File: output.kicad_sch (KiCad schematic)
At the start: 72 parts, among them Q10 AO4407A, Q11 2N7002, Q12 MMBT3904, Q13 2N7002, Q14 2N7002, Q15 2N7002, Q16 2N7002, Q17 2N7002, Q18 MMBT3904, Q19 AO4407A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

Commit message: Fix incorrect part number on R32
Previously chosen part had 0402 footprint, 0603 needed.
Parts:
- R32: LCSC C25792 -> C25819
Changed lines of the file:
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@@
       (effects (font (size 1.27 1.27)) hide)
     )
-    (property "LCSC" "C25792" (id 4) (at 102.87 119.38 0)
+    (property "LCSC" "C25819" (id 4) (at 102.87 119.38 0)
       (effects (font (size 1.27 1.27)) hide)
     )

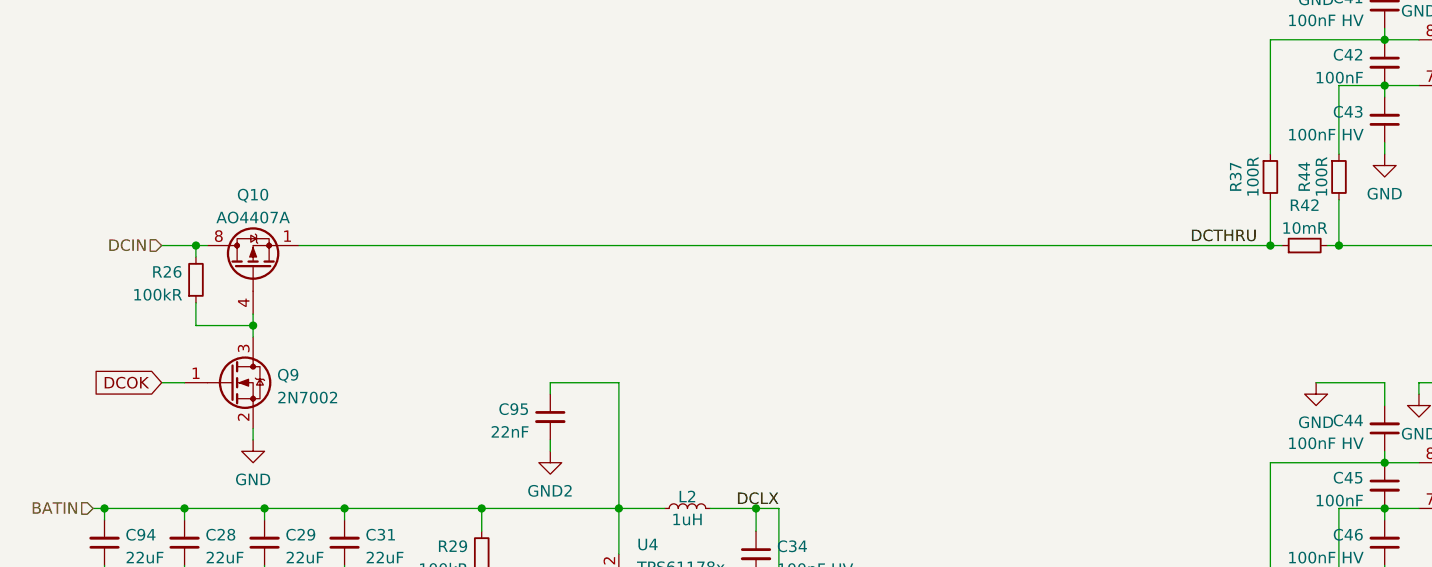
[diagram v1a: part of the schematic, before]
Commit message: Fix gate discharge resistor on Q10
The gate discharge resistor on Q10 was by mistake connected to drain
instead of source.
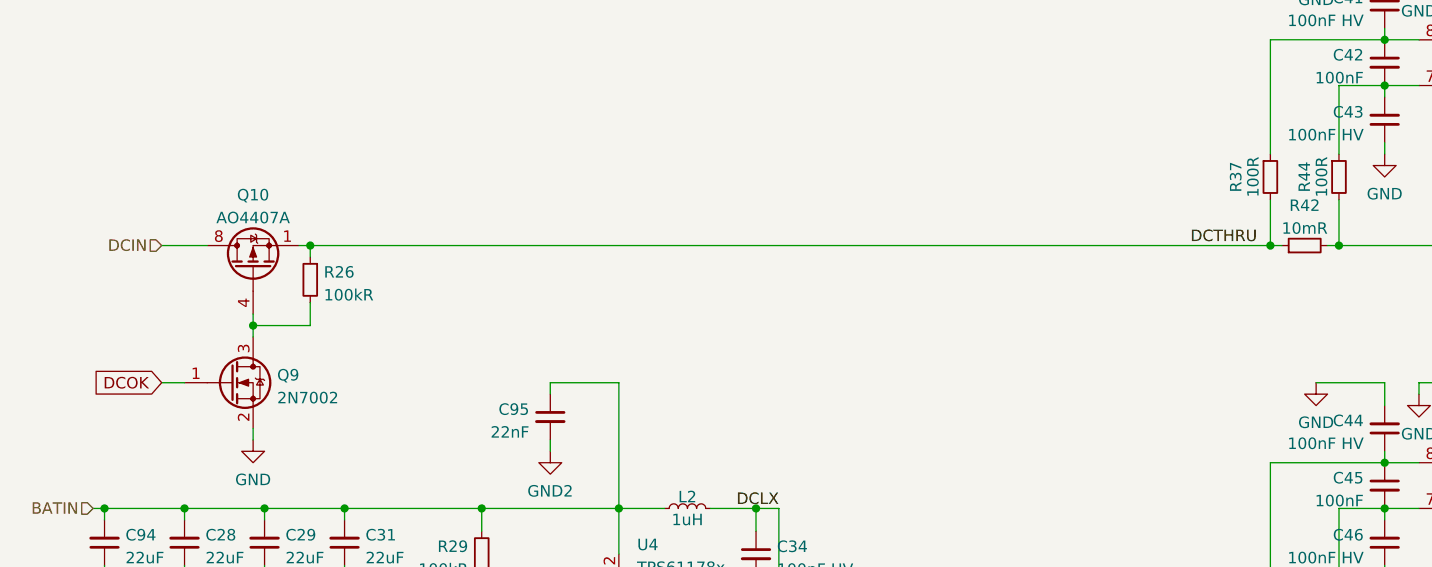
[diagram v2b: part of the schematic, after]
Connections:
- net DCIN: no longer R26.2
- net DCTHRU: now also R26.1
- net at Q10.4 (G), Q9.3 (D): now also R26.2; no longer R26.1
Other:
- moved on the sheet: R26
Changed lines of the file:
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@@
   (junction (at 186.69 104.14) (diameter 0) (color 0 0 0 0)
   )
+  (junction (at 48.26 66.04) (diameter 0) (color 0 0 0 0)
+  )
+  (junction (at 54.61 57.15) (diameter 0) (color 0 0 0 0)
+  )
   (junction (at 223.52 57.15) (diameter 0) (color 0 0 0 0)
   )
   (junction (at 104.14 86.36) (diameter 0) (color 0 0 0 0)
   )
-  (junction (at 48.26 66.04) (diameter 0) (color 0 0 0 0)
-  )
   (junction (at 198.12 113.03) (diameter 0) (color 0 0 0 0)
   )
@@
   )
   (junction (at 198.12 104.14) (diameter 0) (color 0 0 0 0)
-  )
-  (junction (at 41.91 57.15) (diameter 0) (color 0 0 0 0)
   )
   (junction (at 105.41 143.51) (diameter 0) (color 0 0 0 0)
@@
     (stroke (width 0) (type default) (color 0 0 0 0))
   )
+  (wire (pts (xy 54.61 66.04) (xy 54.61 63.5))
+    (stroke (width 0) (type default) (color 0 0 0 0))
+  )
   (wire (pts (xy 58.42 129.54) (xy 87.63 129.54))
     (stroke (width 0) (type default) (color 0 0 0 0))
@@
     (stroke (width 0) (type default) (color 0 0 0 0))
   )
-  (wire (pts (xy 38.1 57.15) (xy 41.91 57.15))
-    (stroke (width 0) (type default) (color 0 0 0 0))
-  )
   (wire (pts (xy 173.99 25.4) (xy 173.99 27.94))
     (stroke (width 0) (type default) (color 0 0 0 0))
@@
     (stroke (width 0) (type default) (color 0 0 0 0))
   )
-  (wire (pts (xy 41.91 66.04) (xy 48.26 66.04))
+  (wire (pts (xy 54.61 57.15) (xy 161.29 57.15))
     (stroke (width 0) (type default) (color 0 0 0 0))
   )
@@
     (stroke (width 0) (type default) (color 0 0 0 0))
   )
-  (wire (pts (xy 41.91 63.5) (xy 41.91 66.04))
-    (stroke (width 0) (type default) (color 0 0 0 0))
-  )
-  (wire (pts (xy 53.34 57.15) (xy 161.29 57.15))
-    (stroke (width 0) (type default) (color 0 0 0 0))
-  )
-  (wire (pts (xy 41.91 58.42) (xy 41.91 57.15))
+  (wire (pts (xy 53.34 57.15) (xy 54.61 57.15))
     (stroke (width 0) (type default) (color 0 0 0 0))
   )
@@
     (stroke (width 0) (type default) (color 0 0 0 0))
   )
-  (wire (pts (xy 41.91 57.15) (xy 43.18 57.15))
+  (wire (pts (xy 38.1 57.15) (xy 43.18 57.15))
     (stroke (width 0) (type default) (color 0 0 0 0))
   )
@@
     (stroke (width 0) (type default) (color 0 0 0 0))
   )
+  (wire (pts (xy 54.61 57.15) (xy 54.61 58.42))
+    (stroke (width 0) (type default) (color 0 0 0 0))
+  )
   (wire (pts (xy 201.93 83.82) (xy 201.93 88.9))
     (stroke (width 0) (type default) (color 0 0 0 0))
@@
     (stroke (width 0) (type default) (color 0 0 0 0))
   )
-  (wire (pts (xy 48.26 66.04) (xy 48.26 64.77))
+  (wire (pts (xy 48.26 64.77) (xy 48.26 66.04))
     (stroke (width 0) (type default) (color 0 0 0 0))
   )
@@
     (stroke (width 0) (type default) (color 0 0 0 0))
   )
+  (wire (pts (xy 48.26 66.04) (xy 48.26 67.31))
+    (stroke (width 0) (type default) (color 0 0 0 0))
+  )
   (wire (pts (xy 73.66 114.3) (xy 73.66 115.57))
     (stroke (width 0) (type default) (color 0 0 0 0))
@@
     (stroke (width 0) (type default) (color 0 0 0 0))
   )
+  (wire (pts (xy 48.26 66.04) (xy 54.61 66.04))
+    (stroke (width 0) (type default) (color 0 0 0 0))
+  )
   (wire (pts (xy 198.12 113.03) (xy 208.28 113.03))
     (stroke (width 0) (type default) (color 0 0 0 0))
@@
   )
   (wire (pts (xy 198.12 81.28) (xy 200.66 81.28))
-    (stroke (width 0) (type default) (color 0 0 0 0))
-  )
-  (wire (pts (xy 48.26 66.04) (xy 48.26 67.31))
     (stroke (width 0) (type default) (color 0 0 0 0))
   )
@@
     (pin "3")
   )
-  (symbol (lib_id "Device:R_Small") (at 41.91 60.96 0) (mirror x) (unit 1)
-    (in_bom yes) (on_board yes) (fields_autoplaced)
-    (property "Reference" "R26" (id 0) (at 40.4115 60.1253 0)
-      (effects (font (size 1.27 1.27)) (justify right))
-    )
-    (property "Value" "100kR" (id 1) (at 40.4115 62.6622 0)
-      (effects (font (size 1.27 1.27)) (justify right))
-    )
-    (property "Footprint" "Resistor_SMD:R_0402_1005Metric" (id 2) (at 41.91 60.96 0)
-      (effects (font (size 1.27 1.27)) hide)
-    )
-    (property "Datasheet" "~" (id 3) (at 41.91 60.96 0)
-      (effects (font (size 1.27 1.27)) hide)
-    )
-    (property "LCSC" "C25741" (id 4) (at 41.91 60.96 0)
-      (effects (font (size 1.27 1.27)) hide)
-    )
+  (symbol (lib_id "Device:R_Small") (at 54.61 60.96 0) (mirror y) (unit 1)
+    (in_bom yes) (on_board yes) (fields_autoplaced)
+    (property "Reference" "R26" (id 0) (at 56.1086 60.1253 0)
+      (effects (font (size 1.27 1.27)) (justify right))
+    )
+    (property "Value" "100kR" (id 1) (at 56.1086 62.6622 0)
+      (effects (font (size 1.27 1.27)) (justify right))
+    )
+    (property "Footprint" "Resistor_SMD:R_0402_1005Metric" (id 2) (at 54.61 60.96 0)
+      (effects (font (size 1.27 1.27)) hide)
+    )
+    (property "Datasheet" "~" (id 3) (at 54.61 60.96 0)
+      (effects (font (size 1.27 1.27)) hide)
+    )
+    (property "LCSC" "C25741" (id 4) (at 54.61 60.96 0)
+      (effects (font (size 1.27 1.27)) hide)
+    )

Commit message: Add ase discharge resistor to Q18
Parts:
- added R?: 100kR, Resistor_SMD:R_0402_1005Metric, symbol Device:R_Small
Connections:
- net GND: now also R?.2
- net at Q18.1 (B), R46.2: now also R?.1
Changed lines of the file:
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@@
   (junction (at 161.29 57.15) (diameter 0) (color 0 0 0 0)
   )
+  (junction (at 186.69 144.78) (diameter 0) (color 0 0 0 0)
+  )
   (junction (at 49.53 137.16) (diameter 0) (color 0 0 0 0)
   )
@@
   )
   (junction (at 143.51 133.35) (diameter 0) (color 0 0 0 0)
+  )
+  (junction (at 194.31 151.13) (diameter 0) (color 0 0 0 0)
   )
   (junction (at 86.36 120.65) (diameter 0) (color 0 0 0 0)
@@
     (stroke (width 0) (type default) (color 0 0 0 0))
   )
+  (wire (pts (xy 186.69 151.13) (xy 194.31 151.13))
+    (stroke (width 0) (type default) (color 0 0 0 0))
+  )
   (wire (pts (xy 31.75 92.71) (xy 31.75 93.98))
     (stroke (width 0) (type default) (color 0 0 0 0))
@@
   )
   (wire (pts (xy 49.53 86.36) (xy 58.42 86.36))
+    (stroke (width 0) (type default) (color 0 0 0 0))
+  )
+  (wire (pts (xy 186.69 144.78) (xy 186.69 146.05))
     (stroke (width 0) (type default) (color 0 0 0 0))
   )
@@
     (pin "1")
   )
+  (symbol (lib_id "Device:R_Small") (at 186.69 148.59 0) (mirror y) (unit 1)
+    (in_bom yes) (on_board yes) (fields_autoplaced)
+    (property "Reference" "R?" (id 0) (at 188.1886 147.7553 0)
+      (effects (font (size 1.27 1.27)) (justify right))
+    )
+    (property "Value" "100kR" (id 1) (at 188.1886 150.2922 0)
+      (effects (font (size 1.27 1.27)) (justify right))
+    )
+    (property "Footprint" "Resistor_SMD:R_0402_1005Metric" (id 2) (at 186.69 148.59 0)
+      (effects (font (size 1.27 1.27)) hide)
+    )
+    (property "Datasheet" "~" (id 3) (at 186.69 148.59 0)
+      (effects (font (size 1.27 1.27)) hide)
+    )
+    (property "LCSC" "C25741" (id 4) (at 186.69 148.59 0)
+      (effects (font (size 1.27 1.27)) hide)
+    )
+    (pin "1")
+    (pin "2")
+  )
   (symbol (lib_id "power:GND") (at 233.68 64.77 0) (unit 1)

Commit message: Fix swapped gauage current sense pins
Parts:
- gave numbers to parts that had none: 1
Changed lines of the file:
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@@
   (symbol (lib_id "Device:R_Small") (at 186.69 148.59 0) (mirror y) (unit 1)
     (in_bom yes) (on_board yes) (fields_autoplaced)
-    (property "Reference" "R?" (id 0) (at 188.1886 147.7553 0)
+    (property "Reference" "R131" (id 0) (at 188.1886 147.7553 0)
       (effects (font (size 1.27 1.27)) (justify right))
     )

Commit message: Fix incorrect AO447A partnumber
The previous partnumber was pointing to a N-Channel MOSFET.
Use a P-Channel one.
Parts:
- Q10, Q19, Q21: LCSC C35349 -> C167517
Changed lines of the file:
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@@
       (effects (font (size 1.27 1.27)) (justify left) hide)
     )
-    (property "LCSC" "C35349" (id 4) (at 208.28 106.68 0)
+    (property "LCSC" "C167517" (id 4) (at 208.28 106.68 0)
       (effects (font (size 1.27 1.27)) hide)
     )
@@
       (effects (font (size 1.27 1.27)) (justify left) hide)
     )
-    (property "LCSC" "C35349" (id 4) (at 48.26 59.69 0)
+    (property "LCSC" "C167517" (id 4) (at 48.26 59.69 0)
       (effects (font (size 1.27 1.27)) hide)
     )
@@
       (effects (font (size 1.27 1.27)) (justify left) hide)
     )
-    (property "LCSC" "C35349" (id 4) (at 193.04 106.68 0)
-      (effects (font (size 1.27 1.27)) hide)
-    )
+    (property "LCSC" "C167517" (id 4) (at 193.04 106.68 0)
+      (effects (font (size 1.27 1.27)) hide)
+    )

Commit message: Rev 1.0 bugfixes
Changes:
 - Replace DCOK-driven DC passthrough switch with ideal diode
 - Reduce INA219 series filter resistance to 1 ohm
 - Simplify debug USB power gating
 - Fix incorrect USB CC pullups
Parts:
- removed Q9: 2N7002, Package_TO_SOT_SMD:SOT-23, symbol Transistor_FET:2N7002
- added Q24, Q9: MMBT5401, Package_TO_SOT_SMD:SOT-23, symbol Transistor_BJT:MMBT3906
- added R62: 10k, Resistor_SMD:R_0402_1005Metric, symbol Device:R_Small
- added R92: 56kR, Resistor_SMD:R_0402_1005Metric, symbol Device:R_Small
- R37, R38, R44, R45: value 100R -> 1R; LCSC C25076 -> C25086
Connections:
- net DCIN: now also Q9.2 (E)
- net DCTHRU: now also Q24.2 (E); no longer R26.1
- net GND: now also R26.2, R62.2
- net at Q10.4 (G): now also R26.1, Q24.3 (C); no longer R26.2
- new net: Q24.1 (B), Q9.1 (B), Q9.3 (C), R92.2
- new net: R62.1, R92.1
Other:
- moved on the sheet: Q10, R26
